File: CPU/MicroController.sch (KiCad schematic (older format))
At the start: 37 parts, among them J301 Conn_02x03_Odd_Even, Q201 DMC4050, Q302 IRLML0040TR, SW301 TACTILE_SWITCHPTS540-SMD, SW302 TACTILE_SWITCHPTS540-SMD, SW303 TACTILE_SWITCHPTS540-SMD, SW304 TACTILE_SWITCHPTS540-SMD, SW305 TACTILE_SWITCHPTS540-SMD, SW306 TACTILE_SWITCHPTS540-SMD, SW307 TACTILE_SWITCHPTS540-SMD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

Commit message: Added the remaining 3D models to the components. Not all are quite accurate but good for visualization. Credit for the RPiWZ 3D model goes to Kevin Schneider at https://gallery.autodesk.com/fusion360/users/200707241731883.
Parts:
- Q201: footprint Marco:8-SMD -> Package_SO:SO-8_3.9x4.9mm_P1.27mm
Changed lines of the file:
@@
 F 0 "Q201" H 1006 1586 10  0000 R CNN
 F 1 "DMC4050" H 1006 1613 10  0000 R CNN
-F 2 "Marco:8-SMD" H 1550 1600 10  0001 C CNN
+F 2 "Package_SO:SO-8_3.9x4.9mm_P1.27mm" H 1550 1600 10  0001 C CNN
 F 3 "" H 1550 1600 10  0001 C CNN
 F 4 "DMC4050SSD-13" H 1550 1600 50  0001 C CNN "DigiKey"

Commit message: Corrected the issues with v1 of the CPU board. Moved to 0.8mm board. Should be ready for another order.
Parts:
- C301, C303: footprint CPU:C1210 -> Capacitor_SMD:C_0805_2012Metric_Pad1.15x1.40mm_HandSolder
- Y301: footprint Crystal:Resonator-3Pin_W7.0mm_H2.5mm -> Crystal:Resonator_SMD_muRata_CSTxExxV-3Pin_3.0x1.1mm_HandSoldering
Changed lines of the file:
@@
 F 0 "Y301" V 2425 5150 50  0000 C CNN
 F 1 "Resonator_Small" V 2334 5150 50  0000 C CNN
-F 2 "Crystal:Resonator-3Pin_W7.0mm_H2.5mm" H 2075 5200 50  0001 C CNN
+F 2 "Crystal:Resonator_SMD_muRata_CSTxExxV-3Pin_3.0x1.1mm_HandSoldering" H 2075 5200 50  0001 C CNN
 F 3 "~" H 2075 5200 50  0001 C CNN
 F 4 "CSTNE20M0VH3L000R0" H 2100 5200 50  0001 C CNN "DigiKey"
@@
 F 0 "C301" H 6140 5475 59  0000 L BNN
 F 1 "1uF" H 6140 5285 59  0000 L BNN
-F 2 "CPU:C1210" H 6100 5450 50  0001 C CNN
+F 2 "Capacitor_SMD:C_0805_2012Metric_Pad1.15x1.40mm_HandSolder" H 6100 5450 50  0001 C CNN
 F 3 "" H 6100 5450 50  0001 C CNN
 F 4 " C1848 " H 6100 5450 50  0001 C CNN "LCSC Part Number"
@@
 F 0 "C303" H 6440 5475 59  0000 L BNN
 F 1 "10uF" H 6440 5285 59  0000 L BNN
-F 2 "CPU:C1210" H 6400 5450 50  0001 C CNN
+F 2 "Capacitor_SMD:C_0805_2012Metric_Pad1.15x1.40mm_HandSolder" H 6400 5450 50  0001 C CNN
 F 3 "" H 6400 5450 50  0001 C CNN
 F 4 " C13585" H 6400 5450 50  0001 C CNN "LCSC Part Number"

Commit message: Moving signals to accomodate charger sensing.
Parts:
- added R202: 390K, Resistor_SMD:R_0805_2012Metric_Pad1.15x1.40mm_HandSolder, symbol CPU-eagle-import:R-US_R1206
- added R203: 2K, Resistor_SMD:R_0805_2012Metric_Pad1.15x1.40mm_HandSolder, symbol CPU-eagle-import:R-US_R1206
- added TP201, TPRX201, TPTX201: TestPoint, symbol Connector:TestPoint
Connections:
- wire segments 169 -> 183
- no-connect marks 3 -> 2
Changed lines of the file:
@@
 Text HLabel 2400 6400 0    39   Input ~ 0
 85RES
-Text HLabel 2400 6500 0    39   Input ~ 0
+Text HLabel 1050 6500 0    39   Input ~ 0
 CH_STAT
-Text Label 2400 6600 2    39   ~ 0
+Text Label 5700 6300 0    39   ~ 0
 SWM
 Text Label 2400 6800 2    39   ~ 0
@@
 	1600 5000 2400 5000
 Wire Wire Line
-	1450 4800 2400 4800
+	1450 4800 1550 4800
 $Comp
 L Device:Resonator_Small Y?
@@
 	10300 3000 10300 3150
 Connection ~ 10300 3000
-Text Label 1800 6700 2    39   ~ 0
+Text Label 1000 7200 2    39   ~ 0
 PI_PEN_PIN
 Text HLabel 2400 6300 0    39   Input ~ 0
@@
 Text HLabel 2400 6200 0    39   Input ~ 0
 PI_RESET_TOGGLE
-NoConn ~ 5700 6300
-NoConn ~ 1800 6700
-Wire Wire Line
-	700  4900 2400 4900
+NoConn ~ 1000 7200
+Wire Wire Line
+	700  4900 900  4900
 Text Label 2400 6700 2    39   ~ 0
 PI_PWR_SW
+$Comp
+L CPU-eagle-import:R-US_R1206 R?
+U 1 1 5EB5AAED
+P 2000 6500
+AR Path="/5E916134/5EB5AAED" Ref="R?"  Part="1"
+AR Path="/5EB5AAED" Ref="R?"  Part="1"
+AR Path="/5E9D5ED5/5EB5AAED" Ref="R203"  Part="1"
+F 0 "R203" H 1850 6559 59  0000 L BNN
+F 1 "2K" H 1850 6370 59  0000 L BNN
+F 2 "Resistor_SMD:R_0805_2012Metric_Pad1.15x1.40mm_HandSolder" H 2000 6500 50  0001 C CNN
+F 3 "" H 2000 6500 50  0001 C CNN
+F 4 " C17902" H 2000 6500 50  0001 C CNN "LCSC Part Number"
+F 5 "RC1206FR-0710KL" H 2000 6500 50  0001 C CNN "DigiKey"
+	1    2000 6500
+	1    0    0    -1
+$EndComp
+$Comp
+L CPU-eagle-import:R-US_R1206 R?
+U 1 1 5EB66E47
+P 1200 6200
+AR Path="/5E916134/5EB66E47" Ref="R?"  Part="1"
+AR Path="/5EB66E47" Ref="R?"  Part="1"
+AR Path="/5E9D5ED5/5EB66E47" Ref="R202"  Part="1"
+F 0 "R202" H 1050 6259 59  0000 L BNN
+F 1 "390K" H 1050 6070 59  0000 L BNN
+F 2 "Resistor_SMD:R_0805_2012Metric_Pad1.15x1.40mm_HandSolder" H 1200 6200 50  0001 C CNN
+F 3 "" H 1200 6200 50  0001 C CNN
+F 4 " C17902" H 1200 6200 50  0001 C CNN "LCSC Part Number"
+F 5 "RC1206FR-0710KL" H 1200 6200 50  0001 C CNN "DigiKey"
+	1    1200 6200
+	0    -1   -1   0
+$EndComp
+Wire Wire Line
+	2400 6500 2200 6500
+$Comp
+L CPU-eagle-import:5V #SUPPLY?
+U 1 1 5EB7B867
+P 1200 5900
+AR Path="/5EB7B867" Ref="#SUPPLY?"  Part="1"
+AR Path="/5E9D5ED5/5EB7B867" Ref="#SUPPLY0202"  Part="1"
+F 0 "#SUPPLY0202" H 1200 5900 50  0001 C CNN
+F 1 "5V" H 1200 6010 59  0000 C BNN
+F 2 "" H 1200 5900 50  0001 C CNN
+F 3 "" H 1200 5900 50  0001 C CNN
+	1    1200 5900
+	1    0    0    -1
+$EndComp
+Wire Wire Line
+	1200 6000 1200 5900
+Wire Wire Line
+	1800 6500 1200 6500
+Wire Wire Line
+	1200 6400 1200 6500
+Connection ~ 1200 6500
+Wire Wire Line
+	1200 6500 1050 6500
+Wire Wire Line
+	2400 6600 1200 6600
+Wire Wire Line
+	1200 6600 1200 6500
+$Comp
+L Connector:TestPoint TPTX201
+U 1 1 5EBAA904
+P 1300 4450
+F 0 "TPTX201" H 1358 4568 50  0000 L CNN
+F 1 "TestPoint" H 1358 4477 50  0000 L CNN
+F 2 "" H 1500 4450 50  0001 C CNN
+F 3 "~" H 1500 4450 50  0001 C CNN
+	1    1300 4450
+	1    0    0    -1
+$EndComp
+$Comp
+L Connector:TestPoint TPRX201
+U 1 1 5EBAB0CD
+P 900 4450
+F 0 "TPRX201" H 958 4568 50  0000 L CNN
+F 1 "TestPoint" H 958 4477 50  0000 L CNN
+F 2 "" H 1100 4450 50  0001 C CNN
+F 3 "~" H 1100 4450 50  0001 C CNN
+	1    900  4450
+	1    0    0    -1
+$EndComp
+Wire Wire Line
+	1300 4450 1300 4550
+Wire Wire Line
+	1300 4550 1550 4550
+Wire Wire Line
+	1550 4550 1550 4800
+Connection ~ 1550 4800
+Wire Wire Line
+	1550 4800 2400 4800
+Wire Wire Line
+	900  4450 900  4900
+Connection ~ 900  4900
+Wire Wire Line
+	900  4900 2400 4900
+$Comp
+L Connector:TestPoint TP201
+U 1 1 5EBC17A3
+P 3750 1050
+F 0 "TP201" H 3808 1168 50  0000 L CNN
+F 1 "TestPoint" H 3808 1077 50  0000 L CNN
+F 2 "" H 3950 1050 50  0001 C CNN
+F 3 "~" H 3950 1050 50  0001 C CNN
+	1    3750 1050
+	1    0    0    -1
+$EndComp
+$Comp
+L CPU-eagle-import:GND #GND?
+U 1 1 5EBC21E1
+P 3750 1500
+AR Path="/5EBC21E1" Ref="#GND?"  Part="1"
+AR Path="/5E9D5ED5/5EBC21E1" Ref="#GND0106"  Part="1"
+F 0 "#GND0106" H 3750 1500 50  0001 C CNN
+F 1 "GND" H 3750 1500 59  0000 C TNN
+F 2 "" H 3750 1500 50  0001 C CNN
+F 3 "" H 3750 1500 50  0001 C CNN
+	1    3750 1500
+	1    0    0    -1
+$EndComp
+Wire Wire Line
+	3750 1050 3750 1400
 $EndSCHEMATC

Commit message: Updates from CPU v1 were completed. Switched out Tiny84 for a tiny1614 because the 84 lacks a hardware twi driver. This version was sent to production at jlcpcb.
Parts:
- added C206: 100pF, Capacitor_SMD:C_0805_2012Metric_Pad1.15x1.40mm_HandSolder, symbol Device:C
- added C207: 100nF, Capacitor_SMD:C_0805_2012Metric_Pad1.15x1.40mm_HandSolder, symbol CPU-eagle-import:C-USC1210
- added D201: Schottky, Diode_SMD:D_0805_2012Metric_Pad1.15x1.40mm_HandSolder, symbol Device:D_Schottky
- added R204: 1K, Resistor_SMD:R_0805_2012Metric_Pad1.15x1.40mm_HandSolder, symbol CPU-eagle-import:R-US_R1206
- added R205: 10K, Resistor_SMD:R_0805_2012Metric_Pad1.15x1.40mm_HandSolder, symbol CPU-eagle-import:R-US_R1206
- C301: DigiKey C1210F105K3RAC7800 -> C0805F105K3RAC7800; LCSC Part Number C1848 -> C28323
- C303: LCSC Part Number C13585 -> C15850
- R202: DigiKey RC1206FR-0710KL -> RC0805FR-0710KL; LCSC Part Number C17902 -> C17656
- R203: DigiKey RC1206FR-0710KL -> RC0805FR-0710KL; LCSC Part Number C17902 -> C17604
- R208, R209: footprint CPU:R1206 -> Resistor_SMD:R_0805_2012Metric_Pad1.15x1.40mm_HandSolder; DigiKey RC1206FR-0710KL -> RC0805FR-0710KL; LCSC Part Number C17902 -> C17414
- TP201: footprint (none) -> TestPoint:TestPoint_Pad_4.0x4.0mm
- TPRX201, TPTX201: footprint (none) -> TestPoint:TestPoint_Pad_D2.0mm
- U301: LCSC Part Number (none) -> C132230
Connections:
- net labels added: BATT_V
- wire segments 183 -> 186
- no-connect marks 2 -> 8
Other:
- moved on the sheet: C301, C303

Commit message: Add display circuitry.
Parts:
- B301, Q201, R205, R208, R209, TPRX201, TPTX201: Customer Reference (none) -> CR101-V3
- C201: renamed from C304; Customer Reference (none) -> CR101-V3; DigiKey CL21B104KACNNNC -> C0805C104K3RACTU
- C202: renamed from C305; Customer Reference (none) -> CR101-V3; DigiKey CL21B104KACNNNC -> C0805C104K3RACTU
- C203: renamed from C306; Customer Reference (none) -> CR101-V3; DigiKey CL21B104KACNNNC -> C0805C104K3RACTU
- C204: renamed from C307; Customer Reference (none) -> CR101-V3; DigiKey CL21B104KACNNNC -> C0805C104K3RACTU
- C205: renamed from C308; Customer Reference (none) -> CR101-V3; DigiKey CL21B104KACNNNC -> C0805C104K3RACTU
- C206: renamed from C309; Customer Reference (none) -> CR101-V3; DigiKey CL21B104KACNNNC -> C0805C104K3RACTU
- C207: renamed from C310; Customer Reference (none) -> CR101-V3; DigiKey CL21B104KACNNNC -> C0805C104K3RACTU
- C208: renamed from C311; Customer Reference (none) -> CR101-V3; DigiKey CL21B104KACNNNC -> C0805C104K3RACTU
- C209: renamed from C312; Customer Reference (none) -> CR101-V3; DigiKey CL21B104KACNNNC -> C0805C104K3RACTU
- C210: renamed from C313; Customer Reference (none) -> CR101-V3; DigiKey CL21B104KACNNNC -> C0805C104K3RACTU
- C211: renamed from C314; Customer Reference (none) -> CR101-V3; DigiKey CL21B104KACNNNC -> C0805C104K3RACTU
- C212: renamed from C315; Customer Reference (none) -> CR101-V3; DigiKey CL21B104KACNNNC -> C0805C104K3RACTU
- C213: renamed from C316; Customer Reference (none) -> CR101-V3; DigiKey CL21B104KACNNNC -> C0805C104K3RACTU
- C214: renamed from C206; Customer Reference (none) -> CR101-V3; DigiKey CL21B104KACNNNC -> 732-8046-1-ND
- C215: renamed from C207; value 100nF -> 0.1uF; Customer Reference (none) -> CR101-V3; DigiKey C1210F105K3RAC7800 -> C0805C104K3RACTU
- C216: renamed from C301; Customer Reference (none) -> CR101-V3; DigiKey C0805F105K3RAC7800 -> C0805C105K3RACTU
- C217: renamed from C303; Customer Reference (none) -> CR101-V3; DigiKey CL32B106KAJNNNE -> EMK212ABJ106MD-T
- D201: value Schottky -> Zener; symbol Device:D_Schottky -> Device:D_Zener; Customer Reference (none) -> CR101-V3; DigiKey (none) -> UDZVFHTE-174.7BCT-ND
- D312: symbol CPU-eagle-import:DIODE -> Device:D_Schottky; Customer Reference (none) -> CR101-V3; DigiKey (none) -> V1P6-M3/HGICT-ND
- J201: renamed from J301; Customer Reference (none) -> CR101-V3; DigiKey 818-22-006-10-002101, 818-22-006-10-005101 -> 818-22-006-10-002101
- Q202: renamed from Q302; Customer Reference (none) -> CR101-V3
- R202: Customer Reference (none) -> CR101-V3; DigiKey RC0805FR-0710KL -> CRCW0805390KFKEA
- R203: Customer Reference (none) -> CR101-V3; DigiKey RC0805FR-0710KL -> RCG08052K00FKEA
- R204: Customer Reference (none) -> CR101-V3; DigiKey RC0805FR-0710KL -> RC0805FR-071KL
- SW201: renamed from SW301; Customer Reference (none) -> CR101-V3
- SW202: renamed from SW302; Customer Reference (none) -> CR101-V3
- SW203: renamed from SW303; Customer Reference (none) -> CR101-V3
- SW204: renamed from SW304; Customer Reference (none) -> CR101-V3
- SW205: renamed from SW305; Customer Reference (none) -> CR101-V3
- SW206: renamed from SW306; Customer Reference (none) -> CR101-V3
- SW207: renamed from SW307; Customer Reference (none) -> CR101-V3
- SW208: renamed from SW308; Customer Reference (none) -> CR101-V3
- SW209: renamed from SW309; Customer Reference (none) -> CR101-V3
- SW210: renamed from SW310; Customer Reference (none) -> CR101-V3
- SW211: renamed from SW311; Customer Reference (none) -> CR101-V3
- SW212: renamed from SW312; Customer Reference (none) -> CR101-V3
- SW213: renamed from SW313; Customer Reference (none) -> CR101-V3
- TP201: value TestPoint -> GND; Customer Reference (none) -> CR101-V3
- U201: renamed from U301; Customer Reference (none) -> CR101-V3; DigiKey (none) -> ATMEGA328PB-AURCT-ND
- Y201: renamed from Y301; Customer Reference (none) -> CR101-V3
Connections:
- wire segments 186 -> 188
- no-connect marks 8 -> 9
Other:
- moved on the sheet: B301, C201, C202, C203, C204, C205, C206, C207, C208, C209, C210, C211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

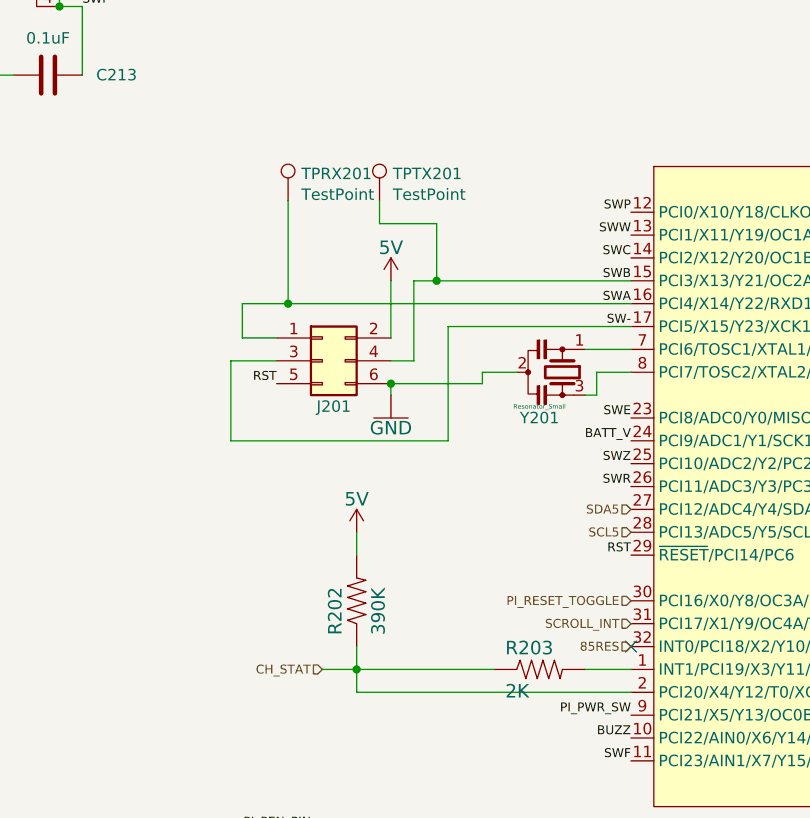
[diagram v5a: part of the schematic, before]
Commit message: Move to separate branch to track CPU development separately.
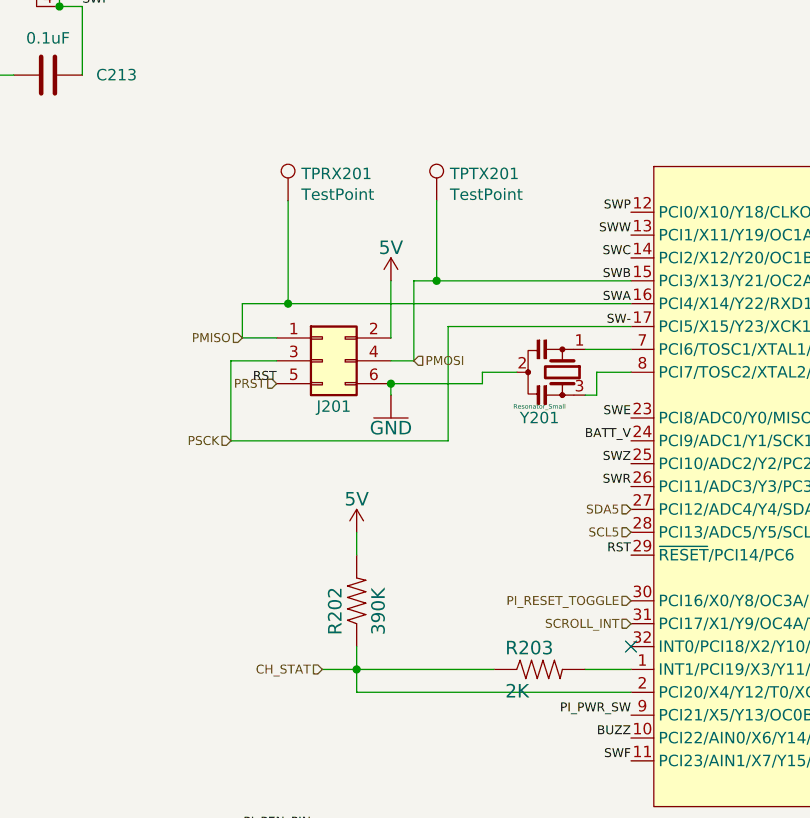
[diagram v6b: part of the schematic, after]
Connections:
- net 85RES: no longer names the net of U201.32 (INT0/PCI18/X2/Y10/OC3B/OC4B/PD2)
- net RST renamed PRST
- net SW- renamed PSCK
- net SWA renamed PMISO
- net SWB renamed PMOSI
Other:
- moved on the sheet: TPTX201
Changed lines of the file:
@@
 Text HLabel 6650 4900 0    39   Input ~ 0
 SCL5
-Text HLabel 6650 5400 0    39   Input ~ 0
-85RES
 Text HLabel 5300 5500 0    39   Input ~ 0
 CH_STAT
@@
 Wire Wire Line
 	5450 5600 5450 5500
-Wire Wire Line
-	5550 3450 5550 3550
-Wire Wire Line
-	5550 3550 5800 3550
-Wire Wire Line
-	5800 3550 5800 3800
 Connection ~ 5800 3800
 Wire Wire Line
@@
 L Connector:TestPoint TPTX201
 U 1 1 5EBAA904
-P 5550 3450
-F 0 "TPTX201" H 5608 3568 50  0000 L CNN
-F 1 "TestPoint" H 5608 3477 50  0000 L CNN
-F 2 "TestPoint:TestPoint_Pad_D2.0mm" H 5750 3450 50  0001 C CNN
-F 3 "~" H 5750 3450 50  0001 C CNN
-F 4 "CR101-V3" H 5550 3450 50  0001 C CNN "Customer Reference"
-	1    5550 3450
+P 5800 3450
+F 0 "TPTX201" H 5858 3568 50  0000 L CNN
+F 1 "TestPoint" H 5858 3477 50  0000 L CNN
+F 2 "TestPoint:TestPoint_Pad_D2.0mm" H 6000 3450 50  0001 C CNN
+F 3 "~" H 6000 3450 50  0001 C CNN
+F 4 "CR101-V3" H 5800 3450 50  0001 C CNN "Customer Reference"
+	1    5800 3450
 	1    0    0    -1
 $EndComp
@@
 Wire Wire Line
 	10400 1350 10400 1500
+Text HLabel 5100 4250 0    39   Input ~ 0
+PRST
+Text HLabel 4950 4050 0    39   Input ~ 0
+PMISO
+Text HLabel 4900 4500 0    39   Input ~ 0
+PSCK
+Text HLabel 5700 4150 2    39   Input ~ 0
+PMOSI
+Wire Wire Line
+	5800 3450 5800 3800
 $EndSCHEMATC

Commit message: Version 4 of the CPU board ordered with this commit.
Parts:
- C201, C202, C203, C204, C205, C206, C207, C208, C209, C210, C211, C212, C213: LCSC Part Number C49678 -> C49678
- C214: LCSC Part Number C49678 -> C1790
- C215: LCSC Part Number C1848 -> C49678
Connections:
- no-connect marks 9 -> 10
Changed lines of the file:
@@
 F 2 "Capacitor_SMD:C_0805_2012Metric_Pad1.15x1.40mm_HandSolder" H 1138 1250 50  0001 C CNN
 F 3 "~" H 1100 1400 50  0001 C CNN
-F 4 " C49678" H 1100 1400 50  0001 C CNN "LCSC Part Number"
+F 4 "C49678" H 1100 1400 50  0001 C CNN "LCSC Part Number"
 F 5 "C0805C104K3RACTU" H 1100 1400 50  0001 C CNN "DigiKey"
 F 6 "CR101-V3" H 1100 1400 50  0001 C CNN "Customer Reference"
@@
 F 2 "Capacitor_SMD:C_0805_2012Metric_Pad1.15x1.40mm_HandSolder" H 1138 2000 50  0001 C CNN
 F 3 "~" H 1100 2150 50  0001 C CNN
-F 4 " C49678" H 1100 2150 50  0001 C CNN "LCSC Part Number"
+F 4 "C49678" H 1100 2150 50  0001 C CNN "LCSC Part Number"
 F 5 "C0805C104K3RACTU" H 1100 2150 50  0001 C CNN "DigiKey"
 F 6 "CR101-V3" H 1100 2150 50  0001 C CNN "Customer Reference"
@@
 F 2 "Capacitor_SMD:C_0805_2012Metric_Pad1.15x1.40mm_HandSolder" H 1138 2700 50  0001 C CNN
 F 3 "~" H 1100 2850 50  0001 C CNN
-F 4 " C49678" H 1100 2850 50  0001 C CNN "LCSC Part Number"
+F 4 "C49678" H 1100 2850 50  0001 C CNN "LCSC Part Number"
 F 5 "C0805C104K3RACTU" H 1100 2850 50  0001 C CNN "DigiKey"
 F 6 "CR101-V3" H 1100 2850 50  0001 C CNN "Customer Reference"
@@
 F 2 "Capacitor_SMD:C_0805_2012Metric_Pad1.15x1.40mm_HandSolder" H 1938 1250 50  0001 C CNN
 F 3 "~" H 1900 1400 50  0001 C CNN
-F 4 " C49678" H 1900 1400 50  0001 C CNN "LCSC Part Number"
+F 4 "C49678" H 1900 1400 50  0001 C CNN "LCSC Part Number"
 F 5 "C0805C104K3RACTU" H 1900 1400 50  0001 C CNN "DigiKey"
 F 6 "CR101-V3" H 1900 1400 50  0001 C CNN "Customer Reference"
@@
 F 2 "Capacitor_SMD:C_0805_2012Metric_Pad1.15x1.40mm_HandSolder" H 1938 1950 50  0001 C CNN
 F 3 "~" H 1900 2100 50  0001 C CNN
-F 4 " C49678" H 1900 2100 50  0001 C CNN "LCSC Part Number"
+F 4 "C49678" H 1900 2100 50  0001 C CNN "LCSC Part Number"
 F 5 "C0805C104K3RACTU" H 1900 2100 50  0001 C CNN "DigiKey"
 F 6 "CR101-V3" H 1900 2100 50  0001 C CNN "Customer Reference"
@@
 F 2 "Capacitor_SMD:C_0805_2012Metric_Pad1.15x1.40mm_HandSolder" H 1938 2700 50  0001 C CNN
 F 3 "~" H 1900 2850 50  0001 C CNN
-F 4 " C49678" H 1900 2850 50  0001 C CNN "LCSC Part Number"
+F 4 "C49678" H 1900 2850 50  0001 C CNN "LCSC Part Number"
 F 5 "C0805C104K3RACTU" H 1900 2850 50  0001 C CNN "DigiKey"
 F 6 "CR101-V3" H 1900 2850 50  0001 C CNN "Customer Reference"
@@
 F 2 "Capacitor_SMD:C_0805_2012Metric_Pad1.15x1.40mm_HandSolder" H 2688 1250 50  0001 C CNN
 F 3 "~" H 2650 1400 50  0001 C CNN
-F 4 " C49678" H 2650 1400 50  0001 C CNN "LCSC Part Number"
+F 4 "C49678" H 2650 1400 50  0001 C CNN "LCSC Part Number"
 F 5 "C0805C104K3RACTU" H 2650 1400 50  0001 C CNN "DigiKey"
 F 6 "CR101-V3" H 2650 1400 50  0001 C CNN "Customer Reference"
@@
 F 2 "Capacitor_SMD:C_0805_2012Metric_Pad1.15x1.40mm_HandSolder" H 2688 1950 50  0001 C CNN
 F 3 "~" H 2650 2100 50  0001 C CNN
-F 4 " C49678" H 2650 2100 50  0001 C CNN "LCSC Part Number"
+F 4 "C49678" H 2650 2100 50  0001 C CNN "LCSC Part Number"
 F 5 "C0805C104K3RACTU" H 2650 2100 50  0001 C CNN "DigiKey"
 F 6 "CR101-V3" H 2650 2100 50  0001 C CNN "Customer Reference"
@@
 F 2 "Capacitor_SMD:C_0805_2012Metric_Pad1.15x1.40mm_HandSolder" H 2688 2700 50  0001 C CNN
 F 3 "~" H 2650 2850 50  0001 C CNN
-F 4 " C49678" H 2650 2850 50  0001 C CNN "LCSC Part Number"
+F 4 "C49678" H 2650 2850 50  0001 C CNN "LCSC Part Number"
 F 5 "C0805C104K3RACTU" H 2650 2850 50  0001 C CNN "DigiKey"
 F 6 "CR101-V3" H 2650 2850 50  0001 C CNN "Customer Reference"
@@
 F 2 "Capacitor_SMD:C_0805_2012Metric_Pad1.15x1.40mm_HandSolder" H 3388 2150 50  0001 C CNN
 F 3 "~" H 3350 2300 50  0001 C CNN
-F 4 " C49678" H 3350 2300 50  0001 C CNN "LCSC Part Number"
+F 4 "C49678" H 3350 2300 50  0001 C CNN "LCSC Part Number"
 F 5 "C0805C104K3RACTU" H 3350 2300 50  0001 C CNN "DigiKey"
 F 6 "CR101-V3" H 3350 2300 50  0001 C CNN "Customer Reference"
@@
 F 2 "Capacitor_SMD:C_0805_2012Metric_Pad1.15x1.40mm_HandSolder" H 4138 1200 50  0001 C CNN
 F 3 "~" H 4100 1350 50  0001 C CNN
-F 4 " C49678" H 4100 1350 50  0001 C CNN "LCSC Part Number"
+F 4 "C49678" H 4100 1350 50  0001 C CNN "LCSC Part Number"
 F 5 "C0805C104K3RACTU" H 4100 1350 50  0001 C CNN "DigiKey"
 F 6 "CR101-V3" H 4100 1350 50  0001 C CNN "Customer Reference"
@@
 F 2 "Capacitor_SMD:C_0805_2012Metric_Pad1.15x1.40mm_HandSolder" H 4238 2000 50  0001 C CNN
 F 3 "~" H 4200 2150 50  0001 C CNN
-F 4 " C49678" H 4200 2150 50  0001 C CNN "LCSC Part Number"
+F 4 "C49678" H 4200 2150 50  0001 C CNN "LCSC Part Number"
 F 5 "C0805C104K3RACTU" H 4200 2150 50  0001 C CNN "DigiKey"
 F 6 "CR101-V3" H 4200 2150 50  0001 C CNN "Customer Reference"
@@
 F 2 "Capacitor_SMD:C_0805_2012Metric_Pad1.15x1.40mm_HandSolder" H 4138 2750 50  0001 C CNN
 F 3 "~" H 4100 2900 50  0001 C CNN
-F 4 " C49678" H 4100 2900 50  0001 C CNN "LCSC Part Number"
+F 4 "C49678" H 4100 2900 50  0001 C CNN "LCSC Part Number"
 F 5 "C0805C104K3RACTU" H 4100 2900 50  0001 C CNN "DigiKey"
 F 6 "CR101-V3" H 4100 2900 50  0001 C CNN "Customer Reference"
@@
 F 2 "Capacitor_SMD:C_0805_2012Metric_Pad1.15x1.40mm_HandSolder" H 10100 4450 50  0001 C CNN
 F 3 "" H 10100 4450 50  0001 C CNN
-F 4 " C1848 " H 10100 4450 50  0001 C CNN "LCSC Part Number"
+F 4 "C49678" H 10100 4450 50  0001 C CNN "LCSC Part Number"
 F 5 "C0805C104K3RACTU" H 10100 4450 50  0001 C CNN "DigiKey"
 F 6 "CR101-V3" H 10100 4450 50  0001 C CNN "Customer Reference"
@@
 F 2 "Capacitor_SMD:C_0805_2012Metric_Pad1.15x1.40mm_HandSolder" H 8388 1850 50  0001 C CNN
 F 3 "~" H 8350 2000 50  0001 C CNN
-F 4 " C49678" H 8350 2000 50  0001 C CNN "LCSC Part Number"
+F 4 "C1790" H 8350 2000 50  0001 C CNN "LCSC Part Number"
 F 5 "732-8046-1-ND" H 8350 2000 50  0001 C CNN "DigiKey"
 F 6 "CR101-V3" H 8350 2000 50  0001 C CNN "Customer Reference"
@@
 Wire Wire Line
 	5800 3450 5800 3800
+NoConn ~ 9900 -1450
 $EndSCHEMATC
